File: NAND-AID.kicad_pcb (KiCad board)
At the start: 2 copper layers, 33.7 x 21.4 mm, 24 parts

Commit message: Fix pad to mask clearance
Signed-off-by: Thomas Rohloff <v10lator@myway.de>
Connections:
- ? pad : 3V3 -> (no net)
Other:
- rule pad_to_mask_clearance: 0 -> 0.08

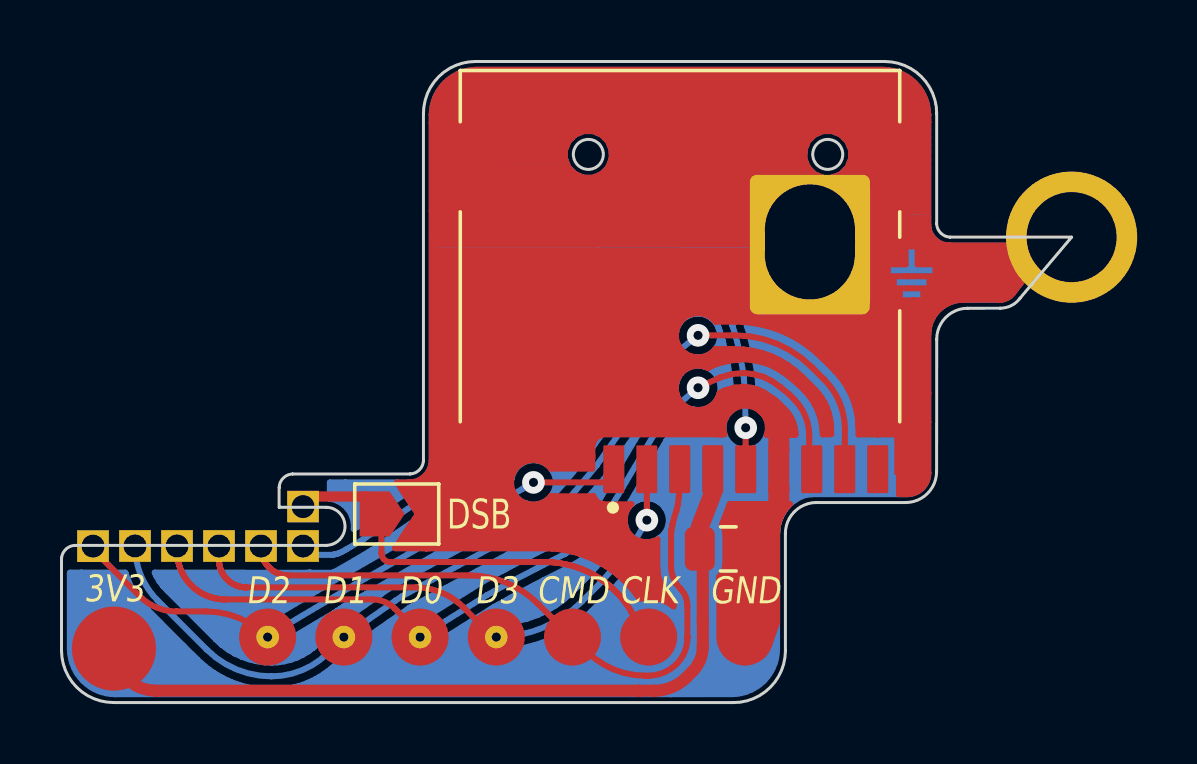
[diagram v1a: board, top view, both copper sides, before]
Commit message: Fix DSB pad
Signed-off-by: Thomas Rohloff <v10lator@myway.de>
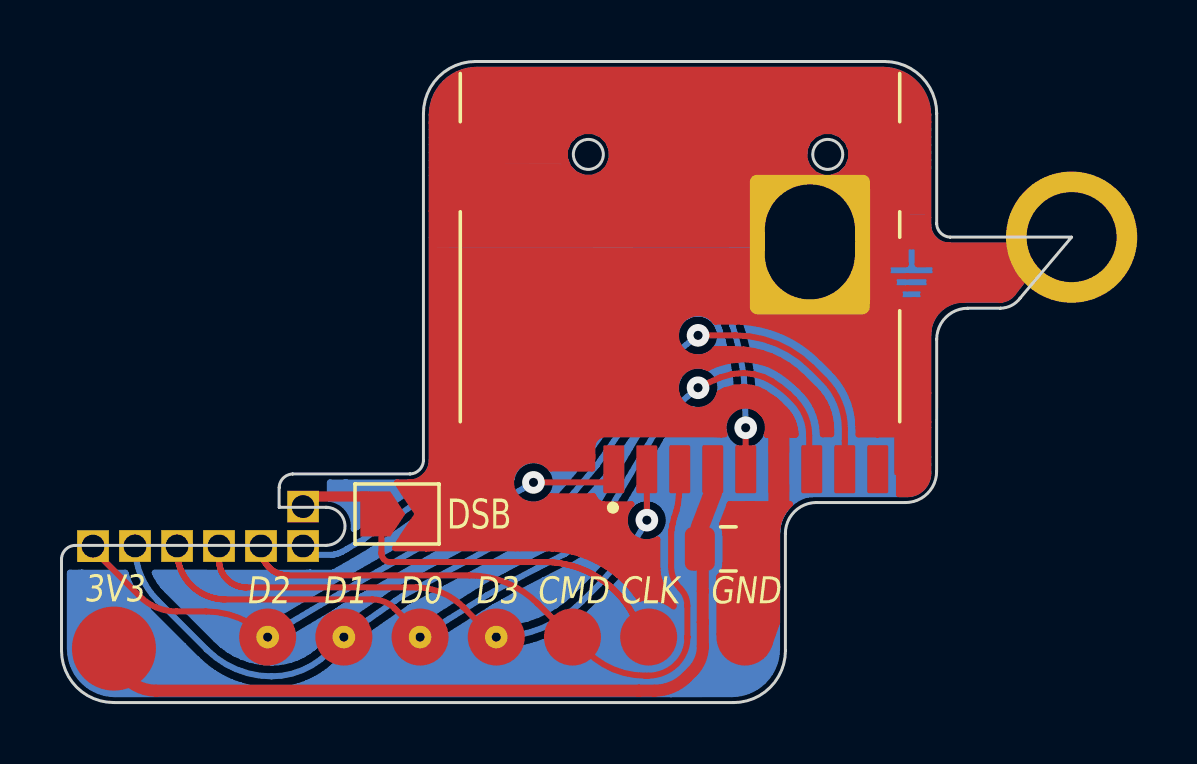
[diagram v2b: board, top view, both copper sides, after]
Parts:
- DSB: value DSB -> SolderJumper-2_P1.3mm_Open_TrianglePad1.0x1.5mm
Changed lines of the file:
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@@
       (net 9 "DUMMY"))
   )
+  (footprint "clipboard:e921f3cf-d82d-49d5-9597-a1b6cd1ad4fa" (layer "F.Cu")
+    (at 134.790931 109.200573)
+    (fp_text reference "" (at 0 0) (layer "F.SilkS")
+        (effects (font (size 1.27 1.27) (thickness 0.15)))
+    )
+    (fp_text value "" (at 0 0) (layer "F.SilkS")
+        (effects (font (size 1.27 1.27) (thickness 0.15)))
+    )
+    (fp_text user "${REFERENCE}" (at 0 0 unlocked) (layer "F.Fab")
+        (effects (font (size 1 1) (thickness 0.15)))
+    )
+    (pad "" thru_hole rect (at 0 -2.5) (size 1.0575 1.0575) (drill 0.762) (property pad_prop_castellated) (layers "*.Cu" "*.Mask")
+      (net 6 "D3"))
+  )
+  (footprint "" (layer "F.Cu")
+    (at 163.21 96.4048)
+    (zone_connect 2)
+    (fp_text reference "" (at 0 0) (layer "F.SilkS")
+        (effects (font (size 1.27 1.27) (thickness 0.15)))
+    )
+    (fp_text value "" (at 0 0) (layer "F.SilkS")
+        (effects (font (size 1.27 1.27) (thickness 0.15)))
+    )
+    (pad "" thru_hole circle (at 0 0) (size 4.375 4.375) (drill 3) (property pad_prop_castellated) (layers "*.Cu" "*.Mask")
+      (net 2 "GND") (pinfunction "Pin_1") (pintype "passive"))
+  )
   (footprint "Jumper:SolderJumper-2_P1.3mm_Open_TrianglePad1.0x1.5mm" (layer "F.Cu")
-    (at 140.715 105.632645)
+    (at 140.72442 105.632053)
     (descr "SMD Solder Jumper, 1x1.5mm Triangular Pads, 0.3mm gap, open")
     (tags "solder jumper open")
-    (attr smd exclude_from_pos_files exclude_from_bom allow_soldermask_bridges)
-    (fp_text reference "DSB" (at 2.744522 0.024358) (layer "F.SilkS" knockout)
+    (attr exclude_from_pos_files exclude_from_bom)
+    (fp_text reference "DSB" (at 2.73558 0.024947) (layer "F.SilkS" knockout)
         (effects (font (size 1 0.75) (thickness 0.15)))
     )
-    (fp_text value "DSB" (at 1.674522 1.9) (layer "F.Fab") hide
+    (fp_text value "SolderJumper-2_P1.3mm_Open_TrianglePad1.0x1.5mm" (at 0 1.9) (layer "F.Fab") hide
         (effects (font (size 1 1) (thickness 0.15)))
     )
@@
     (fp_line (start 1.65 1.25) (end 1.65 -1.25)
       (stroke (width 0.05) (type solid)) (layer "F.CrtYd"))
-    (pad "" smd custom (at -0.735 0) (size 0.3 0.3) (layers "F.Cu" "F.Paste" "F.Mask")
+    (pad "" smd custom (at -0.725 0) (size 0.3 0.3) (layers "F.Cu" "F.Mask")
       (net 9 "DUMMY") (zone_connect 2) (thermal_bridge_angle 45)
       (options (clearance outline) (anchor rect))
@@
           (width 0) (fill yes))
       ))
-    (pad "" smd custom (at 0.735 0) (size 0.3 0.3) (layers "F.Cu" "F.Paste" "F.Mask")
+    (pad "" smd custom (at 0.725 0) (size 0.3 0.3) (layers "F.Cu" "F.Mask")
       (net 2 "GND") (zone_connect 2) (thermal_bridge_angle 45)
       (options (clearance outline) (anchor rect))
@@
           (width 0) (fill yes))
       ))
-  )
-  (footprint "clipboard:e921f3cf-d82d-49d5-9597-a1b6cd1ad4fa" (layer "F.Cu")
-    (at 134.790931 109.200573)
-    (fp_text reference "" (at 0 0) (layer "F.SilkS")
-        (effects (font (size 1.27 1.27) (thickness 0.15)))
-    )
-    (fp_text value "" (at 0 0) (layer "F.SilkS")
-        (effects (font (size 1.27 1.27) (thickness 0.15)))
-    )
-    (fp_text user "${REFERENCE}" (at 0 0 unlocked) (layer "F.Fab")
-        (effects (font (size 1 1) (thickness 0.15)))
-    )
-    (pad "" thru_hole rect (at 0 -2.5) (size 1.0575 1.0575) (drill 0.762) (property pad_prop_castellated) (layers "*.Cu" "*.Mask")
-      (net 6 "D3"))
-  )
-  (footprint "" (layer "F.Cu")
-    (at 163.21 96.4048)
-    (zone_connect 2)
-    (fp_text reference "" (at 0 0) (layer "F.SilkS")
-        (effects (font (size 1.27 1.27) (thickness 0.15)))
-    )
-    (fp_text value "" (at 0 0) (layer "F.SilkS")
-        (effects (font (size 1.27 1.27) (thickness 0.15)))
-    )
-    (pad "" thru_hole circle (at 0 0) (size 4.375 4.375) (drill 3) (property pad_prop_castellated) (layers "*.Cu" "*.Mask")
-      (net 2 "GND") (pinfunction "Pin_1") (pintype "passive"))
   )
   (footprint "clipboard:b2c655aa-6d01-4d7f-99fb-ee2fad09d9e9" (layer "F.Cu")
@@
         (effects (font (size 1 1) (thickness 0.15)))
     )
-    (fp_line (start -7 -8.21) (end -7 -6.5)
-      (stroke (width 0.12) (type default)) (layer "F.SilkS"))
-    (fp_line (start -7 -8.21) (end 7.65 -8.21)
+    (fp_line (start -7 -8.11) (end -7 -6.5)
       (stroke (width 0.12) (type default)) (layer "F.SilkS"))
     (fp_line (start -7 -3.5) (end -7 3.5)
       (stroke (width 0.12) (type default)) (layer "F.SilkS"))
-    (fp_line (start 7.65 -8.21) (end 7.65 -6.5)
+    (fp_line (start 7.65 -8.11) (end 7.65 -6.5)
       (stroke (width 0.12) (type default)) (layer "F.SilkS"))
     (fp_line (start 7.65 -3.5) (end 7.65 -2.65)

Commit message: Small fixes
Signed-off-by: Thomas Rohloff <v10lator@myway.de>
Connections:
- ? pad : (no net) -> 3V3
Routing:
- net GND: track 3438.7 -> 3447.8 mm
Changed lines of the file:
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@@
         (effects (font (size 1 1) (thickness 0.15)))
     )
-    (pad "" smd circle (at -1.3 0) (size 2.8 2.8) (layers "F.Cu" "F.Paste" "F.Mask"))
+    (pad "" smd circle (at -1.3 0) (size 2.8 2.8) (layers "F.Cu" "F.Paste" "F.Mask")
+      (net 1 "3V3"))
   )
   (footprint "" (layer "F.Cu")
@@
   (segment (start 157.106075 92.544313) (end 158.430969 92.544313) (width 0.2) (layer "F.Cu") (net 2))
   (segment (start 146.360586 105.206521) (end 145.897971 105.213358) (width 0.2) (layer "F.Cu") (net 2))
+  (segment (start 145.836806 96.738042) (end 152.565118 96.753368) (width 0.2) (layer "F.Cu") (net 2))
   (segment (start 158.430999 92.584481) (end 158.430999 92.324349) (width 0.2) (layer "F.Cu") (net 2))
   (segment (start 159.138943 97.587672) (end 158.934973 97.791892) (width 0.2) (layer "F.Cu") (net 2))
@@
   (segment (start 153.704 105.407315) (end 152.469736 105.459617) (width 0.2) (layer "F.Cu") (net 2))
   (segment (start 146.890656 106.521389) (end 146.928942 106.625306) (width 0.2) (layer "F.Cu") (net 2))
+  (segment (start 143.90136 93.972647) (end 146.283613 93.987352) (width 0.2) (layer "F.Cu") (net 2))
   (segment (start 153.172618 99.395978) (end 153.555071 99.533133) (width 0.2) (layer "F.Cu") (net 2))
   (segment (start 146.64512 94.329) (end 146.94103 94.45168) (width 0.254) (layer "F.Cu") (net 2))

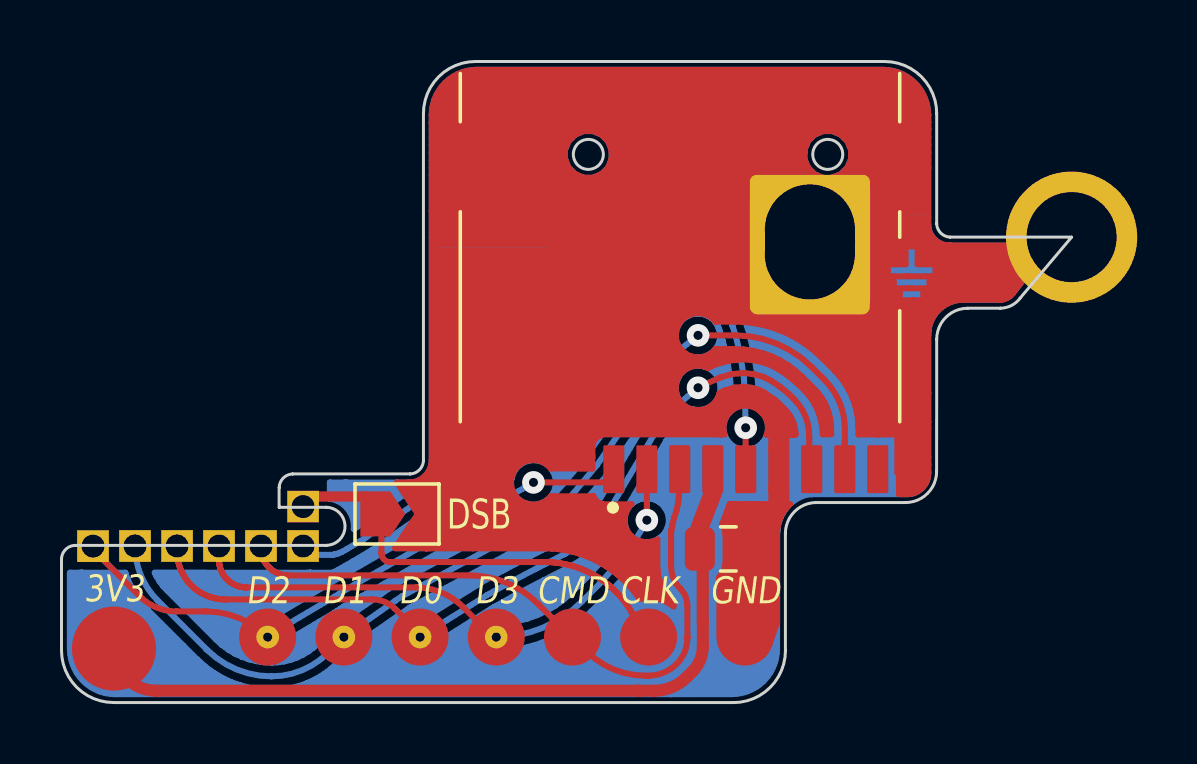
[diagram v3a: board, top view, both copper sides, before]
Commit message: Widen edge
Signed-off-by: Thomas Rohloff <v10lator@myway.de>
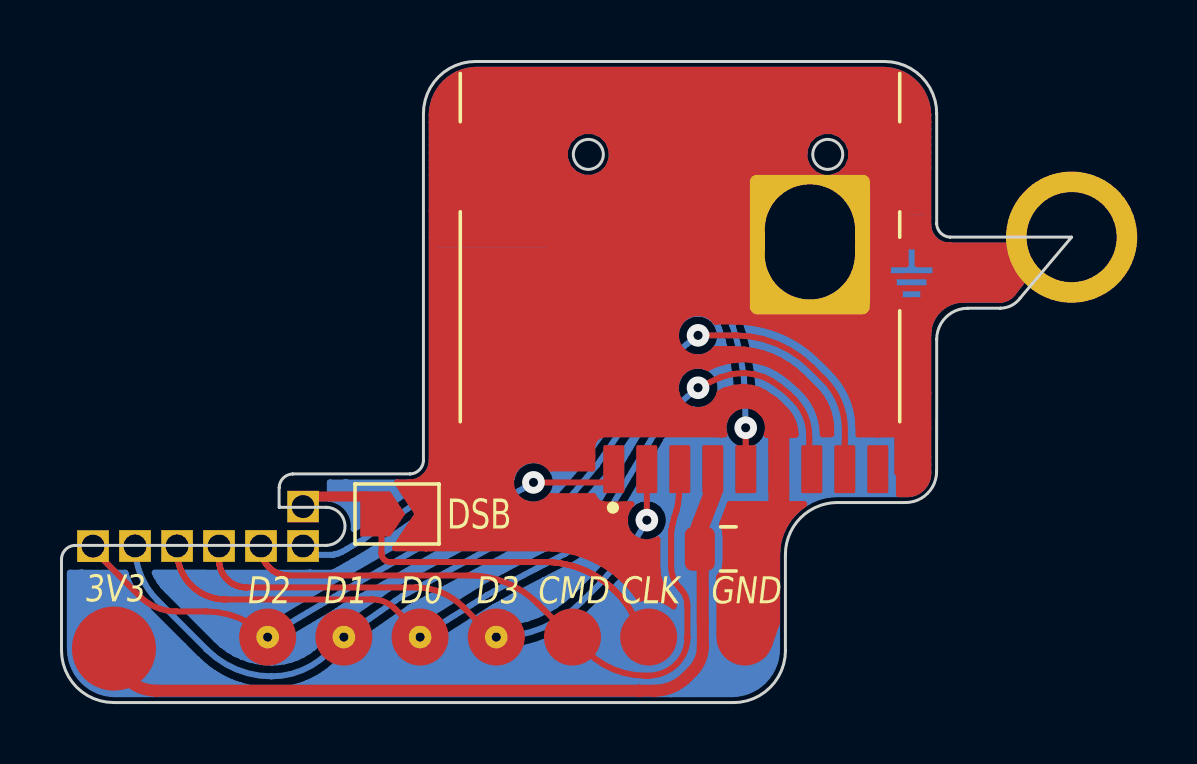
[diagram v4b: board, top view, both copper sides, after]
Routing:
- net GND: track 3447.8 -> 3454.6 mm
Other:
- outline, holes or cut-outs redrawn

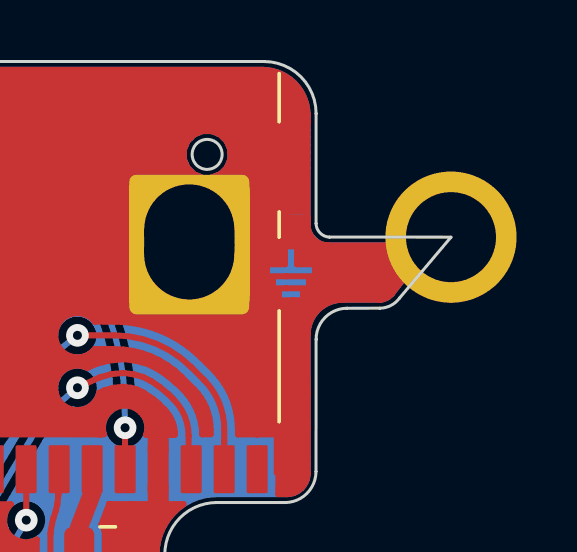
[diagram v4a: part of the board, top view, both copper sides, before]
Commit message: Make copper ring smaller
Signed-off-by: Thomas Rohloff <v10lator@myway.de>
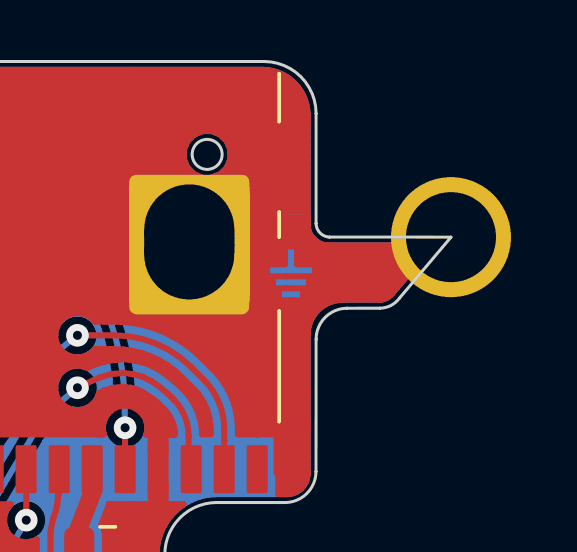
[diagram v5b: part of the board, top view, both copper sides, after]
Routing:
- net GND: track 3454.6 -> 3457.5 mm
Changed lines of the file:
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@@
         (effects (font (size 1.27 1.27) (thickness 0.15)))
     )
-    (pad "" thru_hole circle (at 0 0) (size 4.375 4.375) (drill 3) (property pad_prop_castellated) (layers "*.Cu" "*.Mask")
+    (pad "" thru_hole circle (at 0 0) (size 4 4.375) (drill 3) (property pad_prop_castellated) (layers "*.Cu" "*.Mask")
       (net 2 "GND") (pinfunction "Pin_1") (pintype "passive"))
   )
@@
   (segment (start 142.4612 102.899354) (end 144.099365 102.899354) (width 0.2) (layer "F.Cu") (net 2))
   (segment (start 144.3162 102.65182) (end 144.21815 102.59518) (width 0.254) (layer "F.Cu") (net 2))
-  (segment (start 161.246678 98.281202) (end 161.603743 97.821571) (width 0.2) (layer "F.Cu") (net 2))
   (segment (start 142.27404 92.56776) (end 142.52804 92.56776) (width 0.254) (layer "F.Cu") (net 2))
   (segment (start 141.924572 104.58465) (end 141.389884 104.581501) (width 0.2) (layer "F.Cu") (net 2))
@@
   (segment (start 147.395203 103.066641) (end 147.443439 103.03537) (width 0.2) (layer "F.Cu") (net 2))
   (segment (start 147.226777 106.439144) (end 144.977434 106.368261) (width 0.2) (layer "F.Cu") (net 2))
+  (segment (start 161.631819 97.791771) (end 161.056517 96.887115) (width 0.2) (layer "F.Cu") (net 2))
   (segment (start 154.974303 101.923121) (end 155.053432 102.093247) (width 0.2) (layer "F.Cu") (net 2))
   (segment (start 151.935781 100.136143) (end 152.290539 100.15065) (width 0.2) (layer "F.Cu") (net 2))
@@
   (segment (start 157.77413 95.3577) (end 158.02813 95.3577) (width 0.254) (layer "F.Cu") (net 2))
   (segment (start 152.60415 101.789907) (end 151.613465 101.764586) (width 0.2) (layer "F.Cu") (net 2))
+  (segment (start 161.717365 97.729749) (end 161.231888 96.872144) (width 0.2) (layer "F.Cu") (net 2))
   (segment (start 157.77413 92.56776) (end 158.02813 92.56776) (width 0.254) (layer "F.Cu") (net 2))
   (segment (start 157.08579 95.44203) (end 157.18358 95.49867) (width 0.254) (layer "F.Cu") (net 2))
@@
   (segment (start 153.930232 102.586353) (end 153.916876 102.551373) (width 0.2) (layer "F.Cu") (net 2))
   (segment (start 157.267647 92.7382) (end 158.287862 92.7382) (width 0.2) (layer "F.Cu") (net 2))
+  (segment (start 161.135893 98.144651) (end 161.261951 98.260681) (width 0.2) (layer "F.Cu") (net 2))
   (segment (start 157.085751 94.009625) (end 155.900727 93.993673) (width 0.2) (layer "F.Cu") (net 2))
   (segment (start 141.23 105.918414) (end 140.674 106.750608) (width 0.2) (layer "F.Cu") (net 2))
@@
   (segment (start 152.545074 101.426406) (end 152.763306 101.488404) (width 0.2) (layer "F.Cu") (net 2))
   (segment (start 144.859296 106.235947) (end 144.920728 105.423159) (width 0.2) (layer "F.Cu") (net 2))
+  (segment (start 161.261951 98.260681) (end 161.717365 97.729749) (width 0.2) (layer "F.Cu") (net 2))
   (segment (start 148.900417 101.068107) (end 148.895871 101.786389) (width 0.2) (layer "F.Cu") (net 2))
   (segment (start 142.067638 100.090696) (end 142.067638 101.268135) (width 0.2) (layer "F.Cu") (net 2))
@@
   (segment (start 153.857347 100.766419) (end 153.863017 99.394131) (width 0.2) (layer "B.Cu") (net 2))
   (segment (start 153.005539 103.468996) (end 153.578347 102.683431) (width 0.2) (layer "B.Cu") (net 2))
-  (segment (start 161.240661 98.28739) (end 161.597726 97.827759) (width 0.2) (layer "B.Cu") (net 2))
   (segment (start 152.704379 99.815325) (end 152.867692 100.550236) (width 0.2) (layer "B.Cu") (net 2))
   (segment (start 140.031864 111.141731) (end 141.795749 111.150823) (width 0.2) (layer "B.Cu") (net 2))
@@
   (segment (start 131.274 111.531689) (end 135.865362 111.544545) (width 0.2) (layer "B.Cu") (net 2))
   (segment (start 153.278305 103.283515) (end 153.452875 103.10349) (width 0.2) (layer "B.Cu") (net 2))
+  (segment (start 161.717365 97.729749) (end 161.469537 97.692436) (width 0.2) (layer "B.Cu") (net 2))
   (segment (start 152.456588 94.269052) (end 147.753156 94.252721) (width 0.2) (layer "B.Cu") (net 2))
   (segment (start 148.237025 108.390991) (end 148.098013 108.520888) (width 0.2) (layer "B.Cu") (net 2))
@@
   (segment (start 140.309176 109.991569) (end 140.472835 110.664391) (width 0.2) (layer "B.Cu") (net 2))
   (segment (start 158.637024 98.473774) (end 159.0047 98.502057) (width 0.2) (layer "B.Cu") (net 2))
+  (segment (start 161.469537 97.692436) (end 161.617105 97.536313) (width 0.2) (layer "B.Cu") (net 2))
   (segment (start 147.26133 94.45168) (end 147.55698 94.329) (width 0.254) (layer "B.Cu") (net 2))
   (segment (start 137.698373 111.399175) (end 138.560554 111.000369) (width 0.2) (layer "B.Cu") (net 2))
@@
   (segment (start 150.796085 104.292237) (end 150.869803 104.808263) (width 0.2) (layer "B.Cu") (net 2))
   (segment (start 133.842844 108.150743) (end 136.599392 108.120662) (width 0.2) (layer "B.Cu") (net 2))
+  (segment (start 161.261951 98.260681) (end 161.717365 97.729749) (width 0.2) (layer "B.Cu") (net 2))
   (segment (start 151.862115 97.444282) (end 149.894412 97.70513) (width 0.2) (layer "B.Cu") (net 2))
   (segment (start 150.566772 100.414605) (end 150.455177 100.505122) (width 0.2) (layer "B.Cu") (net 2))
